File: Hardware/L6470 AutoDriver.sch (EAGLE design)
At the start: 39 parts, among them U1 L6470

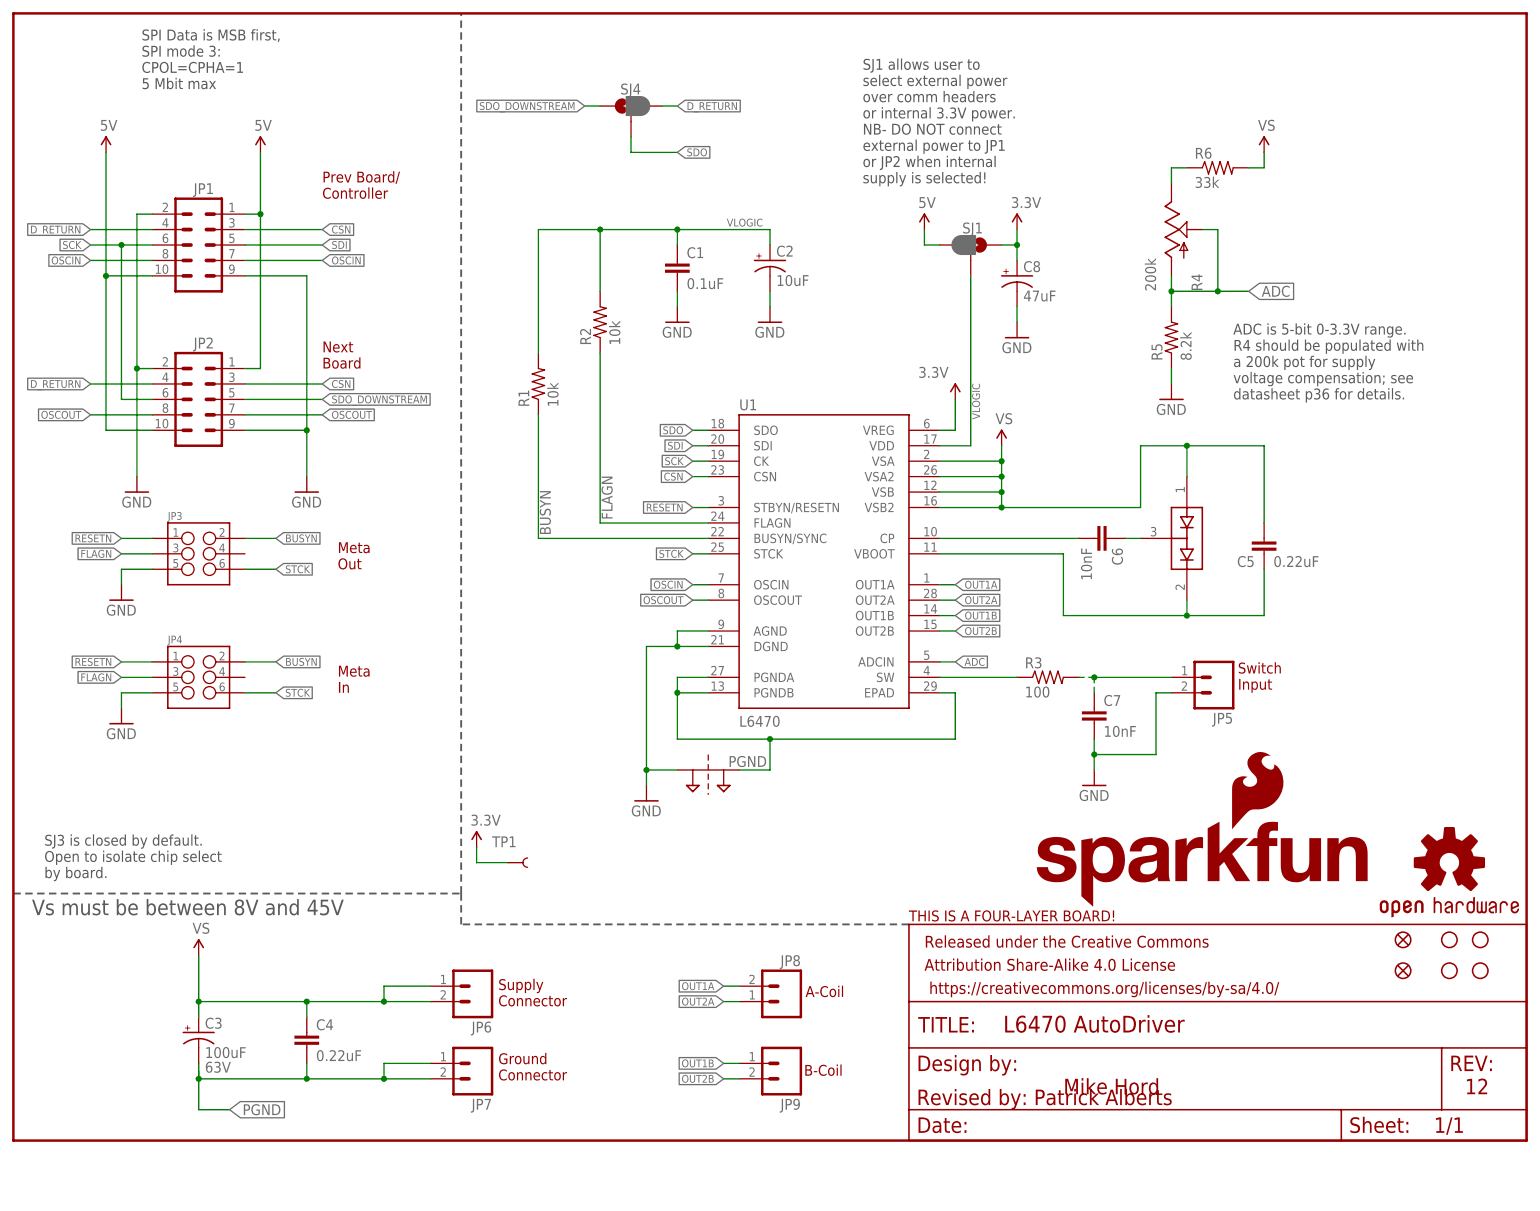
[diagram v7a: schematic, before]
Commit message: Fix minor stuff from QC feedback
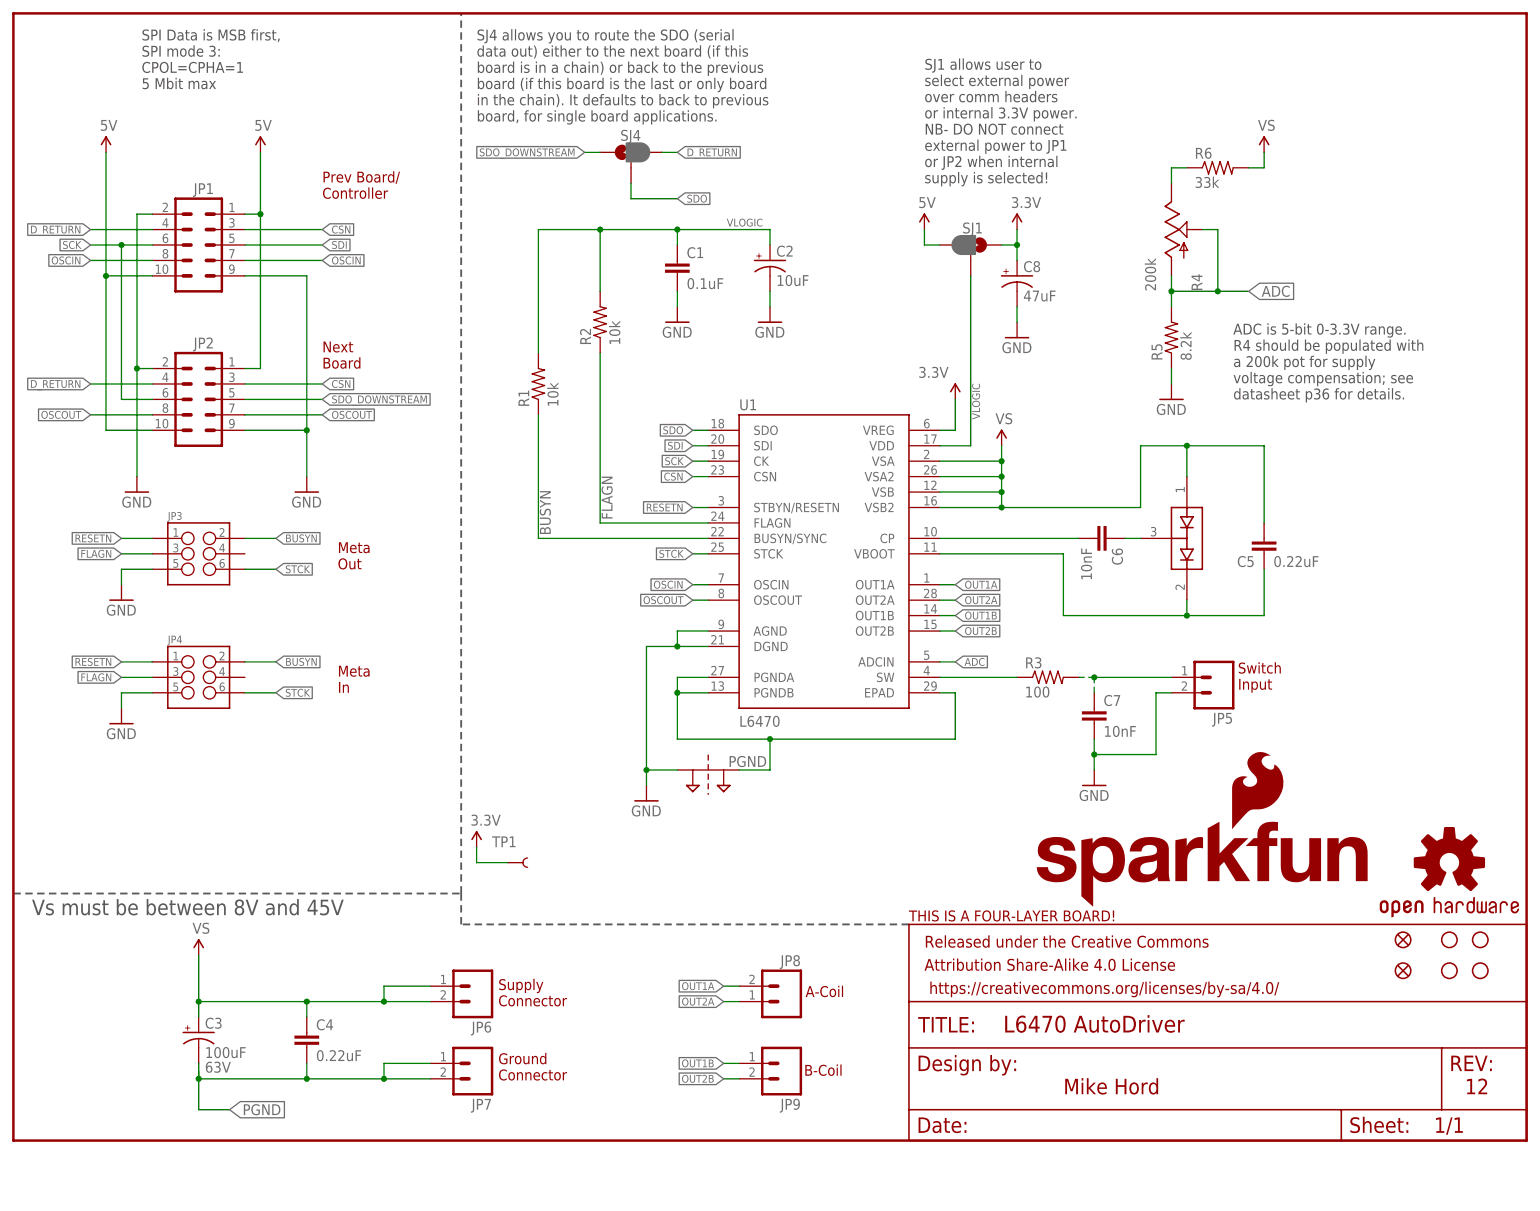
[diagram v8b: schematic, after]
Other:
- note added: "SJ4 allows you to route the SDO (serial data out) either to the next board (if this board is in a chain) or back to the previous board (if this board is the last or only board in the chain). It defaults to back to previous board, for single board applications."
- note removed: "Revised by: Patrick Alberts"
- note removed: "SJ3 is closed by default. Open to isolate chip select by board."
- moved on the sheet: SJ4
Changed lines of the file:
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@@
 <text x="79.756" y="9.906" size="1.778" layer="94">Ground
 Connector</text>
-<text x="139.7" y="157.48" size="1.778" layer="97">SJ1 allows user to
+<text x="149.86" y="157.48" size="1.778" layer="97">SJ1 allows user to
 select external power
 over comm headers
@@
 CPOL=CPHA=1
 5 Mbit max</text>
-<text x="148.59" y="5.842" size="2.54" layer="94">Revised by: Patrick Alberts</text>
 <wire x1="157.48" y1="147.32" x2="154.94" y2="147.32" width="0.508" layer="94"/>
-<text x="5.08" y="43.18" size="1.778" layer="97">SJ3 is closed by default.
-Open to isolate chip select
-by board.</text>
 <wire x1="0" y1="40.64" x2="73.66" y2="40.64" width="0.3048" layer="97" style="longdash"/>
 <wire x1="73.66" y1="40.64" x2="73.66" y2="185.42" width="0.3048" layer="97" style="longdash"/>
@@
 <text x="3.048" y="37.084" size="2.54" layer="97">Vs must be between 8V and 45V</text>
 <text x="238.76" y="7.62" size="2.54" layer="94">12</text>
+<text x="76.2" y="167.64" size="1.778" layer="97">SJ4 allows you to route the SDO (serial
+data out) either to the next board (if this
+board is in a chain) or back to the previous
+board (if this board is the last or only board
+in the chain). It defaults to back to previous
+board, for single board applications.</text>
 </plain>
 <instances>
@@
 <instance part="FRAME1" gate="G$1" x="0" y="0"/>
 <instance part="FRAME1" gate="V" x="147.32" y="0"/>
-<instance part="SJ4" gate="G$1" x="101.6" y="170.18" smashed="yes" rot="R90">
-<attribute name="NAME" x="99.822" y="172.085" size="1.778" layer="95"/>
+<instance part="SJ4" gate="G$1" x="101.6" y="162.56" smashed="yes" rot="R90">
+<attribute name="NAME" x="99.822" y="164.465" size="1.778" layer="95"/>
 </instance>
 </instances>
@@
 <segment>
 <pinref part="SJ4" gate="G$1" pin="3"/>
-<wire x1="106.68" y1="170.18" x2="109.22" y2="170.18" width="0.1524" layer="91"/>
-<label x="109.22" y="170.18" size="1.27" layer="95" xref="yes"/>
+<wire x1="106.68" y1="162.56" x2="109.22" y2="162.56" width="0.1524" layer="91"/>
+<label x="109.22" y="162.56" size="1.27" layer="95" xref="yes"/>
 </segment>
 </net>
@@
 <segment>
 <pinref part="SJ4" gate="G$1" pin="2"/>
-<wire x1="101.6" y1="165.1" x2="101.6" y2="162.56" width="0.1524" layer="91"/>
-<wire x1="101.6" y1="162.56" x2="109.22" y2="162.56" width="0.1524" layer="91"/>
-<label x="109.22" y="162.56" size="1.27" layer="95" xref="yes"/>
+<wire x1="101.6" y1="157.48" x2="101.6" y2="154.94" width="0.1524" layer="91"/>
+<wire x1="101.6" y1="154.94" x2="109.22" y2="154.94" width="0.1524" layer="91"/>
+<label x="109.22" y="154.94" size="1.27" layer="95" xref="yes"/>
 </segment>
 </net>
@@
 <segment>
 <pinref part="SJ4" gate="G$1" pin="1"/>
-<wire x1="96.52" y1="170.18" x2="93.98" y2="170.18" width="0.1524" layer="91"/>
-<label x="93.98" y="170.18" size="1.27" layer="95" rot="R180" xref="yes"/>
-</segment>
-</net>
+<wire x1="96.52" y1="162.56" x2="93.98" y2="162.56" width="0.1524" layer="91"/>
+<label x="93.98" y="162.56" size="1.27" layer="95" rot="R180" xref="yes"/>
+</segment>
+</net>
